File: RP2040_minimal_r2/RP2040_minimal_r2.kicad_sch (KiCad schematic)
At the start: 44 parts, among them J1 SPI0.8, J10 B20, J11 B21, J12 GPIO26-29, J2 SPI0.9, J3 SPI1.13, J4 I²C0, J5 USB, J6 B16, J7 B17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

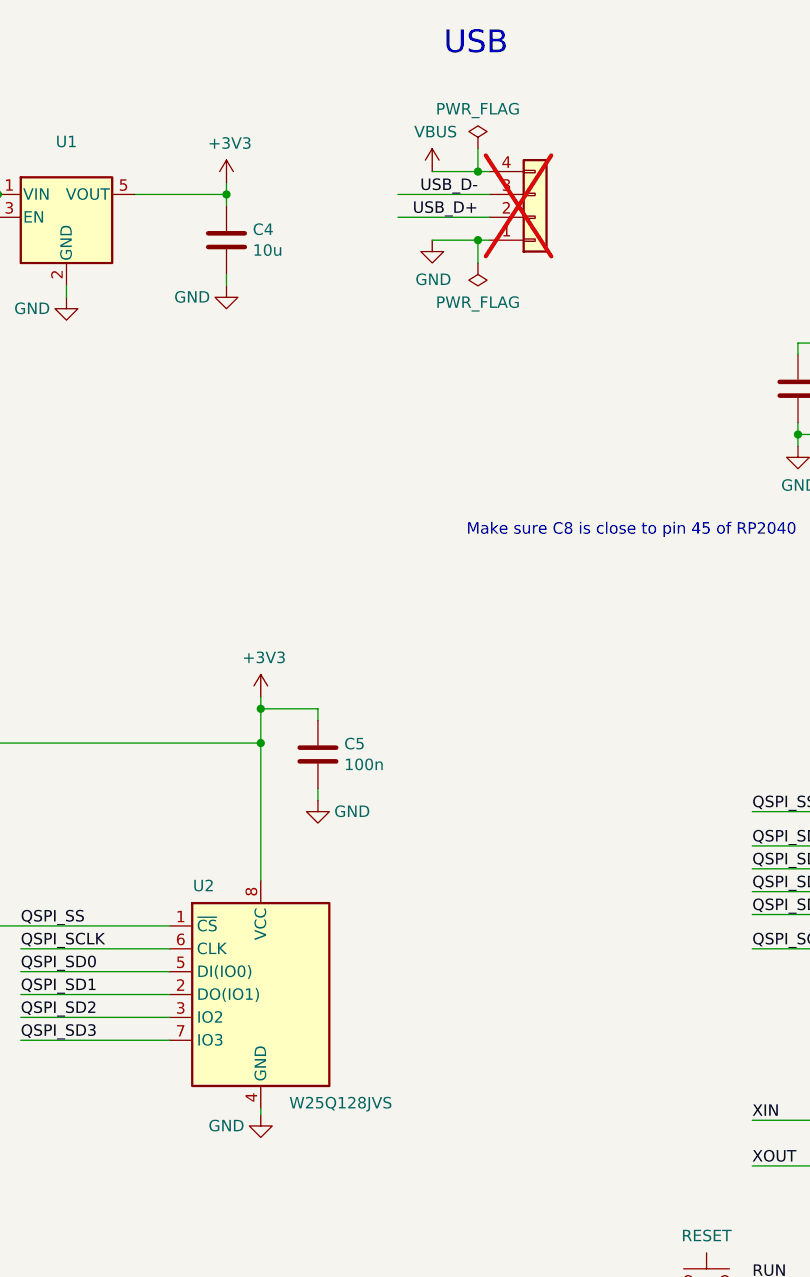
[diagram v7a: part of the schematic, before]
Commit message: Update the USB connection to use a proper JST-XH footprint. Add local copies of several footprints that need to be tweaked to match JLCPCB's notion of component orientation/origin.
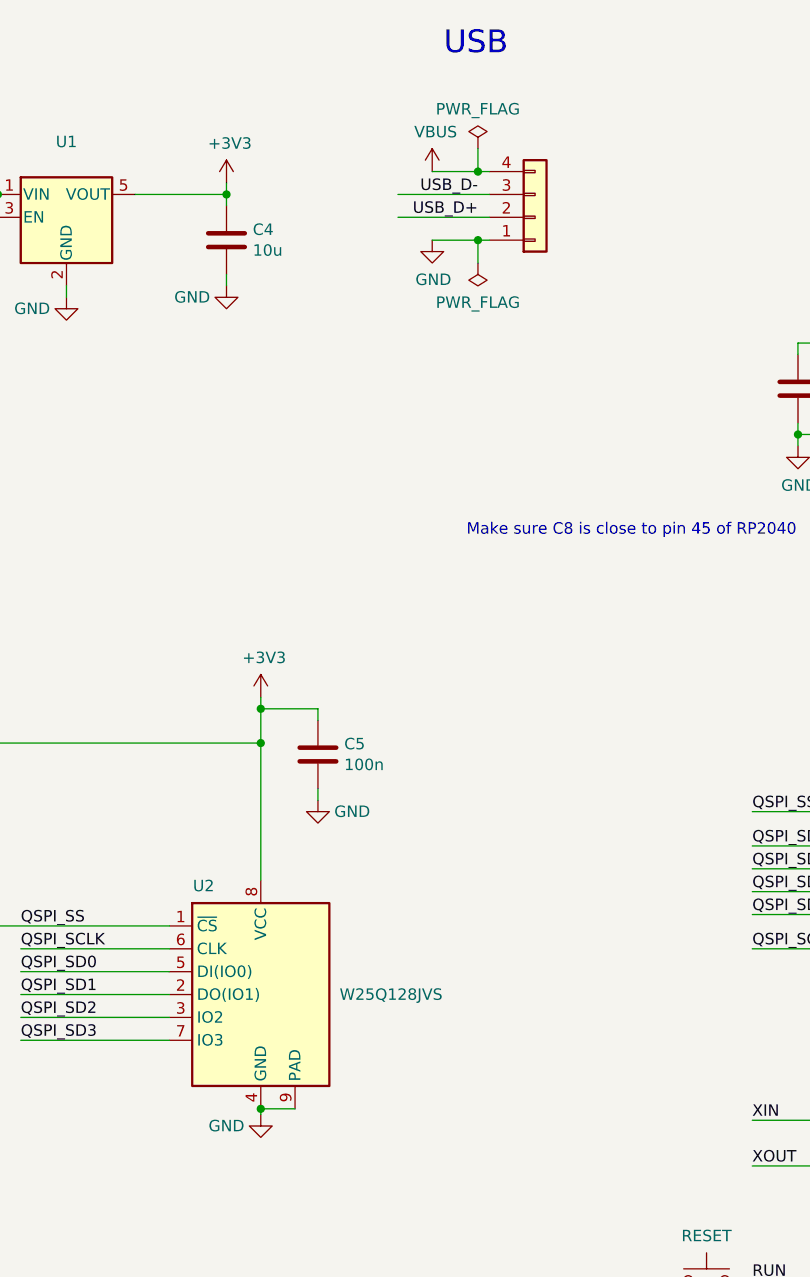
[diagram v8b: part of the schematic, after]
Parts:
- J1, J12, J2, J3: footprint Connector_JST:JST_SH_BM06B-SRSS-TB_1x06-1MP_P1.00mm_Vertical -> RP2040_minimal:JST_SH_BM06B-SRSS-TB_1x06-1MP_P1.00mm_Vertical; LCSC C160392 -> C7430455
- J10, J11, J6, J7, J8, J9: footprint Connector_JST:JST_SH_BM02B-SRSS-TB_1x02-1MP_P1.00mm_Vertical -> RP2040_minimal:JST_SH_BM02B-SRSS-TB_1x02-1MP_P1.00mm_Vertical
- J5: footprint Connector_PinHeader_2.54mm:PinHeader_1x04_P2.54mm_Vertical -> RP2040_minimal:JST_XH_B4B-XH-A_1x04_P2.50mm_Vertical; LCSC (none) -> C7429634; now fitted
- SW1, SW2: LCSC C231329 -> C498294
- U1: footprint Package_TO_SOT_SMD:SOT-23-5 -> RP2040_minimal:SOT-23-5
- U2: footprint Package_SON:WSON-8-1EP_6x5mm_P1.27mm_EP3.4x4.3mm -> RP2040_minimal:WSON-8-1EP_6x5mm_P1.27mm_EP3.4x4.3mm
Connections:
- net GND: now also U2.9 (PAD)
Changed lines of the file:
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@@
 	)
 	(junction
+		(at 97.79 146.05)
+		(diameter 0)
+		(color 0 0 0 0)
+	)
+	(junction
 		(at 66.675 215.9)
 		(diameter 0)
@@
 	(wire
 		(pts
+			(xy 97.79 146.05) (xy 101.6 146.05)
+		)
+		(stroke
+			(width 0)
+			(type default)
+		)
+	)
+	(wire
+		(pts
 			(xy 157.48 71.12) (xy 168.91 71.12)
 		)
@@
 		)
 		(property "Value" "W25Q128JVS"
-			(at 106.68 145.415 0)
+			(at 112.268 133.35 0)
 			(effects
 				(font
@@
 			)
 		)
-		(property "Footprint" "Package_SON:WSON-8-1EP_6x5mm_P1.27mm_EP3.4x4.3mm"
+		(property "Footprint" "RP2040_minimal:WSON-8-1EP_6x5mm_P1.27mm_EP3.4x4.3mm"
 			(at 97.79 110.49 0)
 			(effects
@@
 		(pin "8"
 		)
+		(pin "9"
+		)
 		(instances
 			(project "RP2040_minimal_r2"
@@
 			)
 		)
-		(property "Footprint" "Package_TO_SOT_SMD:SOT-23-5"
+		(property "Footprint" "RP2040_minimal:SOT-23-5"
 			(at 76.2 38.735 0)
 			(effects
@@
 		(in_bom yes)
 		(on_board yes)
-		(dnp yes)
+		(dnp no)
 		(property "Reference" "J5"
 			(at 130.302 46.7868 0)
@@
 			)
 		)
-		(property "Footprint" "Connector_PinHeader_2.54mm:PinHeader_1x04_P2.54mm_Vertical"
+		(property "Footprint" "RP2040_minimal:JST_XH_B4B-XH-A_1x04_P2.50mm_Vertical"
 			(at 128.27 46.99 0)
 			(effects
@@
 			)
 		)
-		(property "LCSC" ""
+		(property "LCSC" "C7429634"
 			(at 128.27 46.99 0)
 			(effects
@@
 			)
 		)
-		(property "LCSC" "C231329"
+		(property "LCSC" "C498294"
 			(at 147.32 165.1 0)
 			(effects
@@
 			)
 		)
-		(property "Footprint" "Connector_JST:JST_SH_BM02B-SRSS-TB_1x02-1MP_P1.00mm_Vertical"
+		(property "Footprint" "RP2040_minimal:JST_SH_BM02B-SRSS-TB_1x02-1MP_P1.00mm_Vertical"
 			(at 328.93 184.15 0)
 			(effects
@@
 			)
 		)
-		(property "Footprint" "Connector_JST:JST_SH_BM06B-SRSS-TB_1x06-1MP_P1.00mm_Vertical"
+		(property "Footprint" "RP2040_minimal:JST_SH_BM06B-SRSS-TB_1x06-1MP_P1.00mm_Vertical"
 			(at 350.52 90.17 0)
 			(effects
@@
 			)
 		)
-		(property "LCSC" "C160392"
+		(property "LCSC" "C7430455"
 			(at 350.52 90.17 0)
 			(effects
@@
 			)
 		)
-		(property "Footprint" "Connector_JST:JST_SH_BM06B-SRSS-TB_1x06-1MP_P1.00mm_Vertical"
+		(property "Footprint" "RP2040_minimal:JST_SH_BM06B-SRSS-TB_1x06-1MP_P1.00mm_Vertical"
 			(at 350.52 115.57 0)
 			(effects
@@
 			)
 		)
-		(property "LCSC" "C160392"
+		(property "LCSC" "C7430455"
 			(at 350.52 115.57 0)
 			(effects
@@
 			)
 		)
-		(property "Footprint" "Connector_JST:JST_SH_BM06B-SRSS-TB_1x06-1MP_P1.00mm_Vertical"
+		(property "Footprint" "RP2040_minimal:JST_SH_BM06B-SRSS-TB_1x06-1MP_P1.00mm_Vertical"
 			(at 285.75 209.55 0)
 			(effects
@@
 			)
 		)
-		(property "LCSC" "C160392"
+		(property "LCSC" "C7430455"
 			(at 285.75 209.55 0)
 			(effects
@@
 			)
 		)
-		(property "LCSC" "C231329"
+		(property "LCSC" "C498294"
 			(at 39.37 125.73 0)
 			(effects
@@
 			)
 		)
-		(property "Footprint" "Connector_JST:JST_SH_BM02B-SRSS-TB_1x02-1MP_P1.00mm_Vertical"
+		(property "Footprint" "RP2040_minimal:JST_SH_BM02B-SRSS-TB_1x02-1MP_P1.00mm_Vertical"
 			(at 328.93 196.85 0)
 			(effects
@@
 			)
 		)
-		(property "Footprint" "Connector_JST:JST_SH_BM02B-SRSS-TB_1x02-1MP_P1.00mm_Vertical"
+		(property "Footprint" "RP2040_minimal:JST_SH_BM02B-SRSS-TB_1x02-1MP_P1.00mm_Vertical"
 			(at 328.93 171.45 0)
 			(effects
@@
 			)
 		)
-		(property "Footprint" "Connector_JST:JST_SH_BM02B-SRSS-TB_1x02-1MP_P1.00mm_Vertical"
+		(property "Footprint" "RP2040_minimal:JST_SH_BM02B-SRSS-TB_1x02-1MP_P1.00mm_Vertical"
 			(at 328.93 212.09 0)
 			(effects
@@
 			)
 		)
-		(property "Footprint" "Connector_JST:JST_SH_BM06B-SRSS-TB_1x06-1MP_P1.00mm_Vertical"
+		(property "Footprint" "RP2040_minimal:JST_SH_BM06B-SRSS-TB_1x06-1MP_P1.00mm_Vertical"
 			(at 350.52 66.04 0)
 			(effects
@@
 			)
 		)
-		(property "LCSC" "C160392"
+		(property "LCSC" "C7430455"
 			(at 350.52 66.04 0)
 			(effects
@@
 			)
 		)
-		(property "Footprint" "Connector_JST:JST_SH_BM02B-SRSS-TB_1x02-1MP_P1.00mm_Vertical"
+		(property "Footprint" "RP2040_minimal:JST_SH_BM02B-SRSS-TB_1x02-1MP_P1.00mm_Vertical"
 			(at 328.93 224.79 0)
 			(effects
@@
 			)
 		)
-		(property "Footprint" "Connector_JST:JST_SH_BM02B-SRSS-TB_1x02-1MP_P1.00mm_Vertical"
+		(property "Footprint" "RP2040_minimal:JST_SH_BM02B-SRSS-TB_1x02-1MP_P1.00mm_Vertical"
 			(at 328.93 156.21 0)
 			(effects
